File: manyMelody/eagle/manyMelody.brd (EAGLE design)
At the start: 74.9 x 95.2 mm, 13 parts, among them IC1 788TV

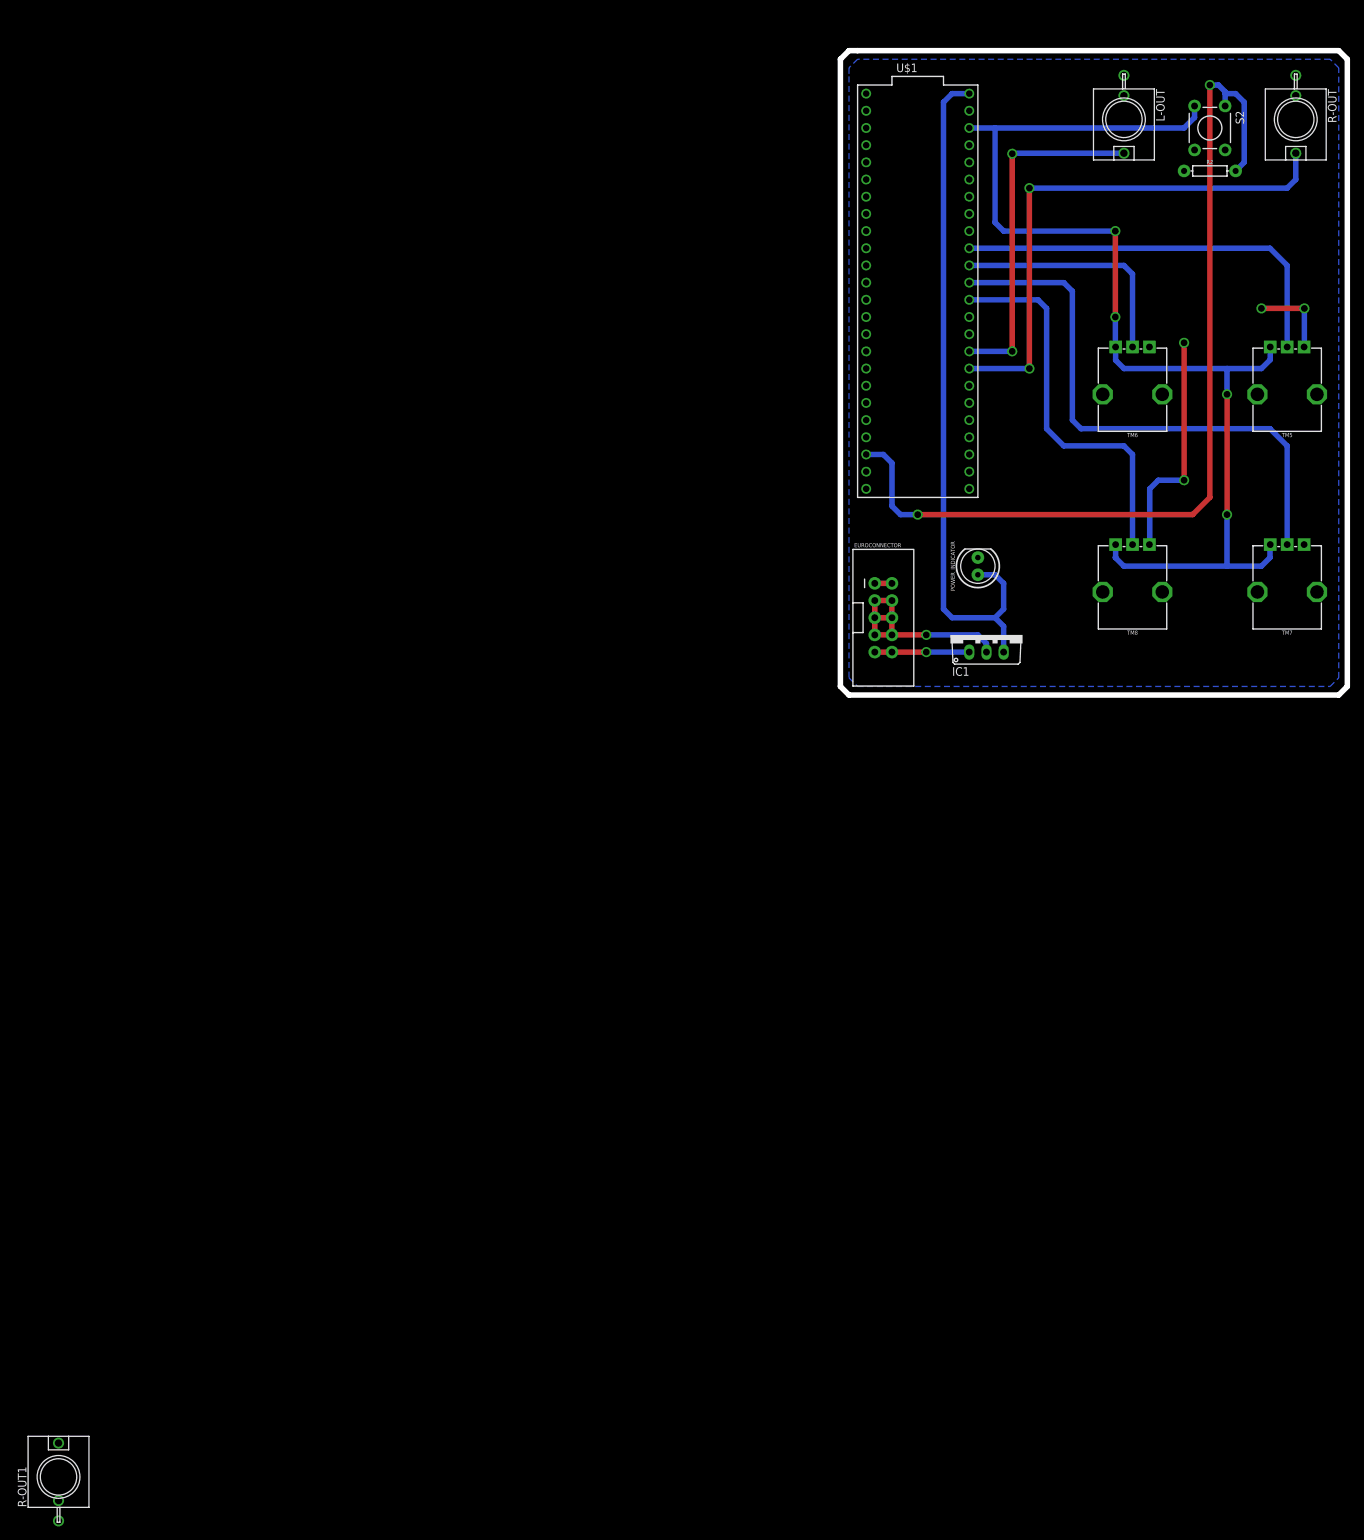
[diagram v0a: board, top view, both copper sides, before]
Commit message: adjusted input pin definitions for teensy and for stereo output
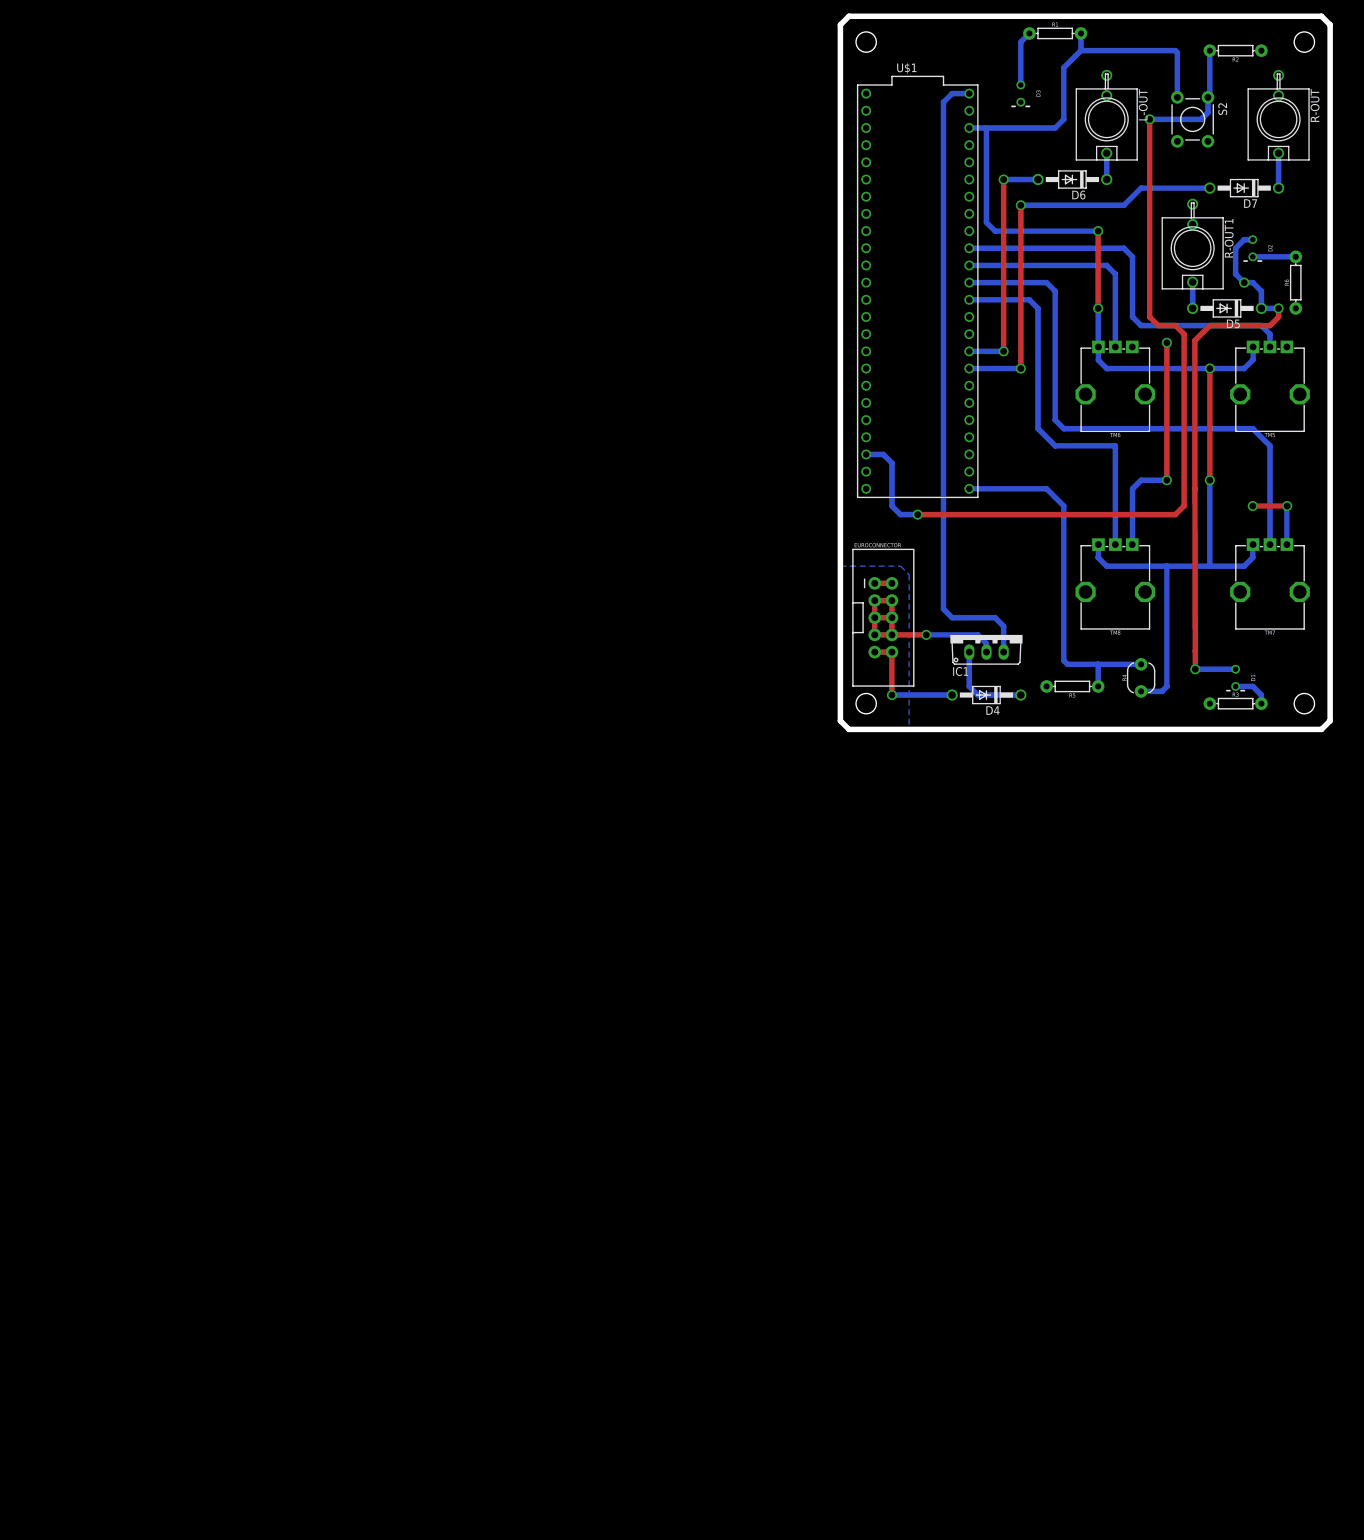
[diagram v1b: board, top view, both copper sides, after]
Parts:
- removed POWER_INDICATOR: (no value), SparkFun-LED:LED_5MM
- added D1, D2, D3: (no value), SparkFun-LED:LED_3MM-NS
- added D4, D5, D6, D7: 1N4148, diode:DO41-10
- added R1: 1k, SparkFun-Resistors:AXIAL-0.3
- added R3, R5, R6: 10k, SparkFun-Resistors:AXIAL-0.3
- added R4: PHOTOCELLPTH-KIT, SparkFun-Sensors:PHOTOCELL-KIT
- moved R-OUT1 247.2 mm to (99.1, 80.0), turned to 180 degrees
- moved R2 18.2 mm to (105.4, 109.2), turned to 180 degrees
- moved S2 2.84 mm to (99.1, 99.1)
- moved L-OUT 2.54 mm to (86.4, 99.1)
- moved TM5 2.54 mm to (110.5, 58.4)
- moved TM6 2.54 mm to (87.6, 58.4)
- moved TM7 2.54 mm to (110.5, 29.2)
- moved TM8 2.54 mm to (87.6, 29.2)
- moved R-OUT 2.54 mm to (111.8, 99.1)
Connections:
- new net N$1: D1.A, D2.A, D5.C
- new net N$15: D4.C, IC1.1
- new net N$16: D5.A, R-OUT1.P$1
- new net N$2: D1.K, R3.P$2
- new net N$4: R4.2, R5.P$1, U$1.33/A14
- new net N$5: D2.K, R6.P$2
- new net N$6: D3.A, R1.P$1
- new net N$7: D6.C, L-OUT.P$1
- new net N$8: D7.C, R-OUT.P$1
- net +12V: now also D4.A; no longer IC1.1
- net 3.3V: now also R1.P$2, R4.1
- net 5V: no longer POWER_INDICATOR.A
- net GND: now also D3.K, R-OUT1.P$3, R3.P$1, R5.P$2, R6.P$1; no longer POWER_INDICATOR.K
- net N$10: now also D7.A; no longer R-OUT.P$1
- net N$9: now also D6.A; no longer L-OUT.P$1
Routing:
- net N$1: track 0.00 -> 86.5 mm, vias 0 -> 3
- net N$4: track 0.00 -> 52.8 mm
- net 3.3V: track 169.8 -> 204.0 mm
- net N$10: track 79.3 -> 60.7 mm
- net N$9: track 52.1 -> 35.6 mm
- net N$15: track 0.00 -> 13.2 mm
- net 5V: track 103.0 -> 93.0 mm
- net N$6: track 0.00 -> 8.15 mm
- net N$5: track 0.00 -> 6.35 mm
- net N$2: track 0.00 -> 5.61 mm
- net N$8: track 0.00 -> 5.16 mm
- net N$3: track 139.0 -> 134.0 mm
- net N$7: track 0.00 -> 3.89 mm
- net N$16: track 0.00 -> 3.89 mm
- net +12V: track 14.0 -> 17.8 mm
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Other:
- board size 74.9 x 95.2 mm -> 72.4 x 105.4 mm
